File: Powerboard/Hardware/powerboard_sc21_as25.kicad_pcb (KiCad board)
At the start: 4 copper layers, 86.3 x 55.6 mm, 152 parts, among them IC1 BQ24618RGET-iclr, IC2 CP2102, J1 Thermistor Connection 103AT N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, J10 Conn_01x04_Male, J11 Conn_01x03_MountingPin, J2 Conn_01x02_Male, J3 Conn_01x02_Male, J4 Conn_01x08_Male, J5 Conn_01x04_Male, J6 Conn_01x02_Male, J7 IsolationSwitch, J8 USB_C_Receptacle_USB2.0, J9 Conn_Coaxial, Q1 RSJ250P10TL, Q10 MCH6351, Q2 RSJ250P10TL, Q3 RSJ250P10TL, Q4 RS1G120MN, Q5 RS1G120MN, Q6 MMDT2222A, Q7 RSJ250P10TL, Q8 RSJ250P10TL, Q9 MCH6351, U1 LTC4412xS6, U11 LTC4411, U2 SN65HVD230, U3 ESP32-PICO-D4, U4 SC4216H, U6 LM2679T-3.3-iclr, U7 LM2679T-3.3-iclr, U8 LTC4412xS6, U9 LTC4412xS6

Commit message: update
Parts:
- moved J7 7.10 mm to (78.6, 78.3), turned to 90 degrees
- moved J6 0.10 mm to (87.8, 71.1)
- moved C44 0.05 mm to (117.8, 69.0)
- moved C48 0.05 mm to (117.8, 70.5)
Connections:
- J7 pad 1: /Battery Charger/Q3-D -> Net-(C31-Pad1)
- J7 pad 2: Net-(C31-Pad1) -> /Battery Charger/Q3-D
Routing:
- net Net-(C31-Pad1): track 38.8 -> 29.7 mm
- net /Battery Charger/Q3-D: track 76.0 -> 74.4 mm, vias 4 -> 3

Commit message: update
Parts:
- added TP1: TestPoint, TestPoint:TestPoint_Pad_D1.5mm, B.Cu at (86.8, 58.0)
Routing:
- net Net-(C31-Pad1): track 29.7 -> 38.9 mm
- net GND: track 103.7 -> 107.9 mm
- net /LPC_24V: track 9.98 -> 12.6 mm
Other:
- board text added: "ISOLATOR"
- board text removed: "ISOLATION SWITCH"

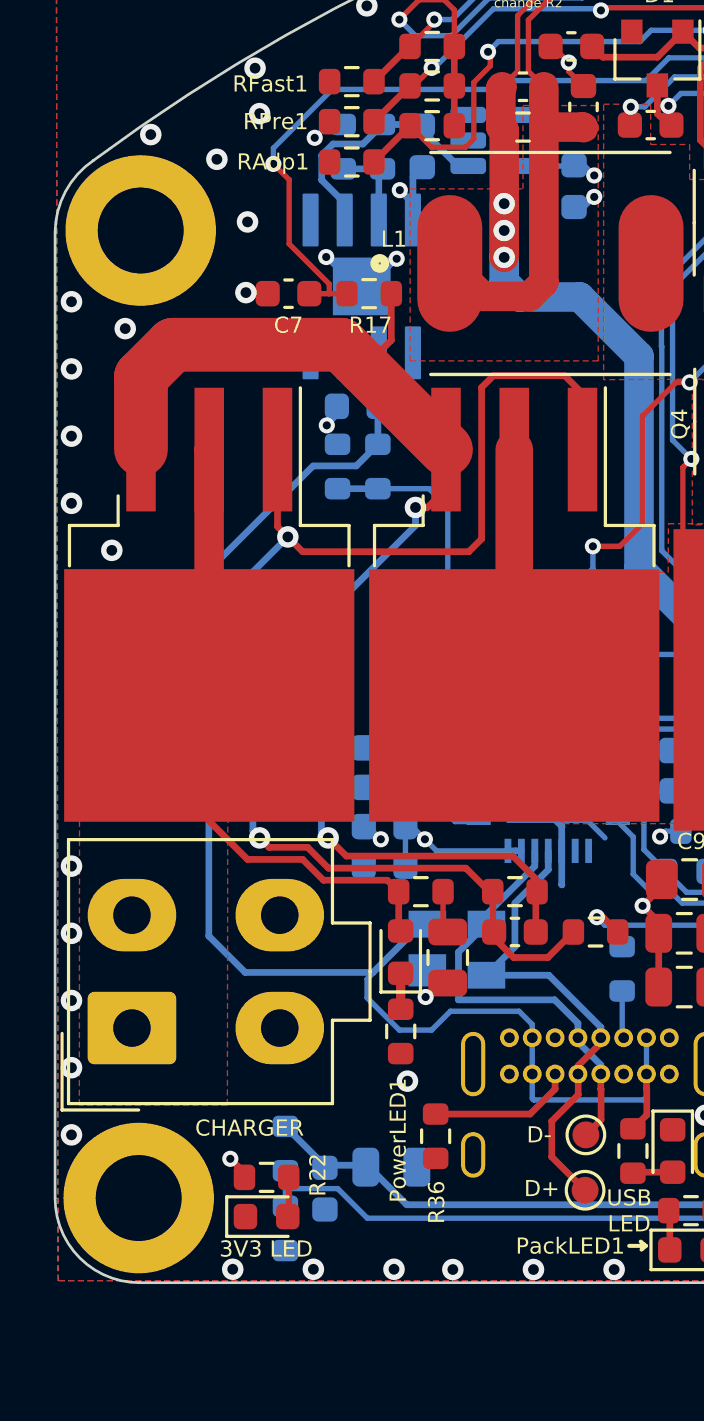
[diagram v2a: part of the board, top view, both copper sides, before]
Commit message: Changed input filter resistors and changed layout to match
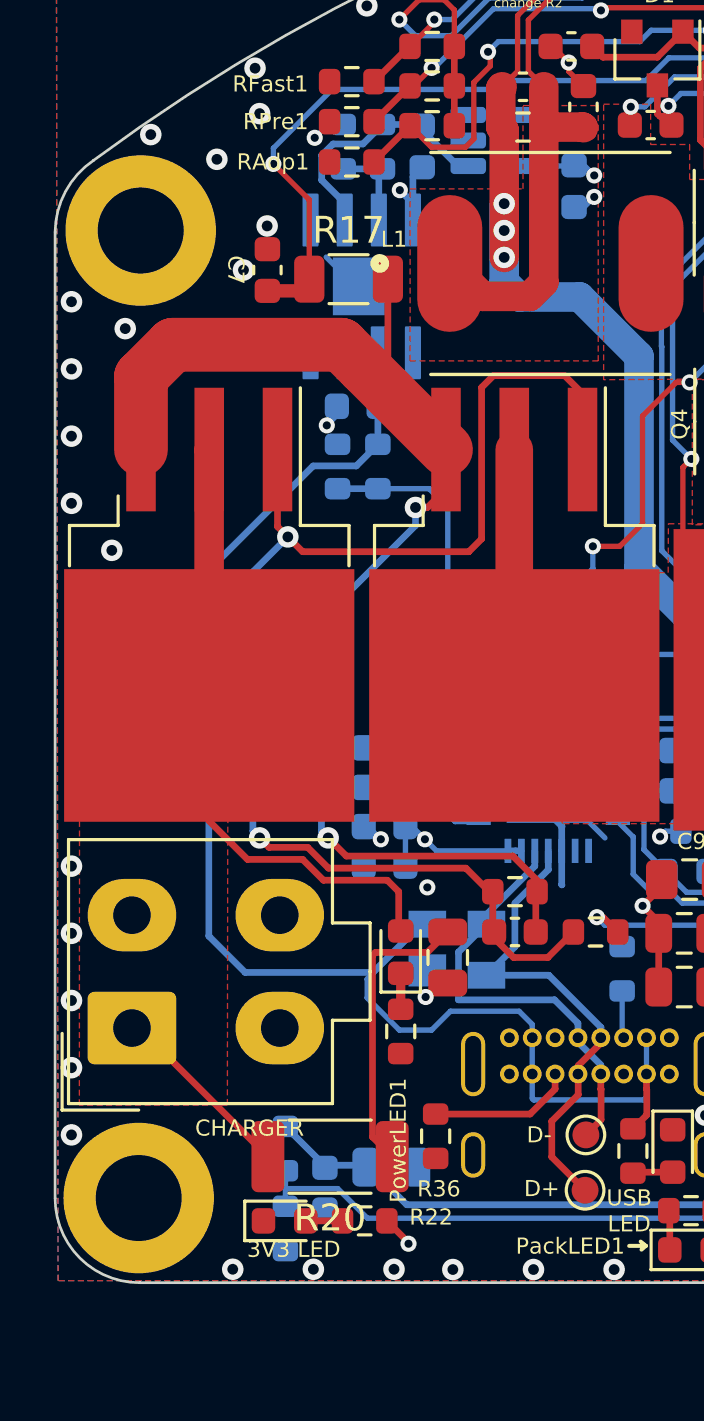
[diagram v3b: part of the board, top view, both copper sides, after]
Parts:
- R17: footprint Resistor_SMD:R_0603_1608Metric -> Resistor_SMD:R_1206_3216Metric
- R20: footprint Resistor_SMD:R_0603_1608Metric -> Resistor_SMD:R_2010_5025Metric
- moved R20 10.4 mm to (59.1, 78.3)
- moved R22 3.99 mm to (60.4, 80.7), turned to 0 degrees
- moved C7 1.18 mm to (56.8, 45.3), turned to -90 degrees
- moved R17 0.94 mm to (59.8, 45.7)
- moved D9 0.69 mm to (57.4, 80.7)
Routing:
- net Net-(C16-Pad1): track 1.33 -> 11.0 mm
- net Net-(J5-Pad1): track 20.9 -> 28.0 mm
- net /Battery Charger/Q1-S: track 44.9 -> 46.0 mm
- net /Battery Charger/VCC: track 30.4 -> 29.9 mm
- net GND: vias 157 -> 155

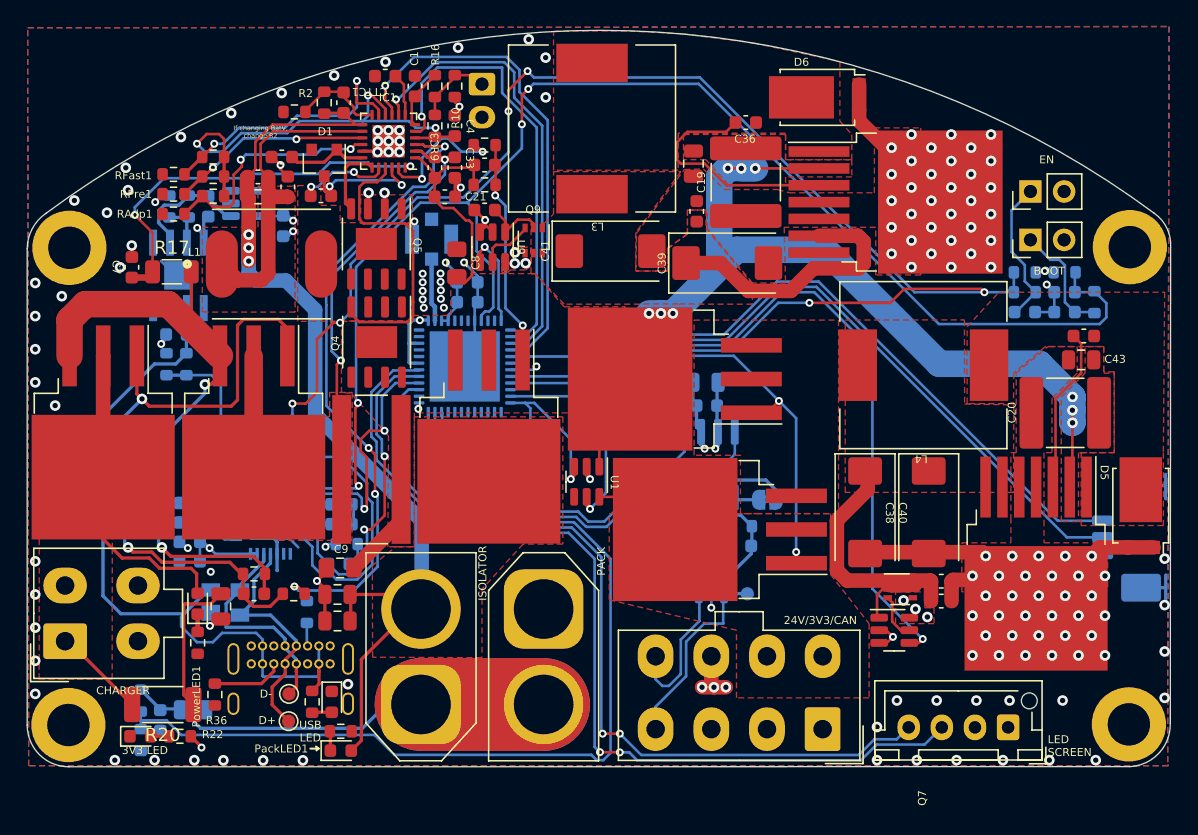
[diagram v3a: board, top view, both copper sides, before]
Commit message: updated pins and new layout
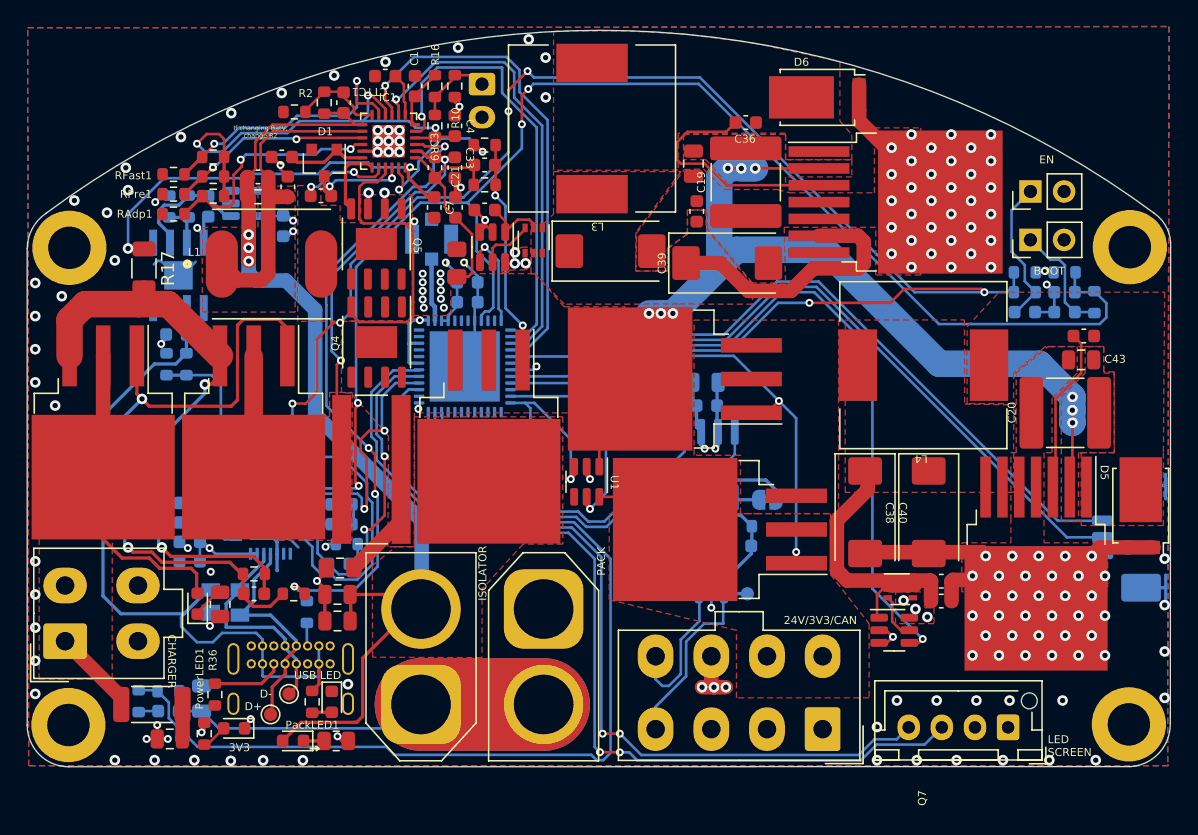
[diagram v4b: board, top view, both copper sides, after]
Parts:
- R28, R29: footprint Resistor_SMD:R_0603_1608Metric -> Resistor_SMD:R_0805_2012Metric
- moved C7 23.3 mm to (79.6, 40.8), turned to 90 degrees
- moved C16 10.7 mm to (59.6, 80.9), turned to 180 degrees
- moved D9 7.10 mm to (64.5, 80.1), turned to 180 degrees
- moved PackLED1 3.67 mm to (69.0, 81.0), turned to 180 degrees
- moved R29 3.36 mm to (63.5, 70.8)
- moved R31 2.93 mm to (57.3, 78.0)
- moved R30 2.21 mm to (59.5, 77.3), turned to 180 degrees
- moved R17 2.13 mm to (57.7, 45.4), turned to -90 degrees
- moved R22 1.85 mm to (62.2, 80.5), turned to 90 degrees
- moved TP24 1.45 mm to (67.2, 79.0)
- moved C21 1.13 mm to (81.2, 40.8), turned to 90 degrees
- moved C32 1.07 mm to (62.0, 77.8), turned to 90 degrees
- moved C31 0.94 mm to (59.5, 78.8), turned to 180 degrees
- moved R20 0.82 mm to (58.3, 78.3)
- moved R28 0.81 mm to (72.2, 81.0)
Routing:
- net Net-(C16-Pad1): track 11.0 -> 2.61 mm
- net GND: track 107.9 -> 113.9 mm, vias 155 -> 159
- net /Battery Charger/Q3-D: track 74.4 -> 78.2 mm
- net /Battery Charger/Q1-S: track 46.0 -> 43.1 mm
- net /Battery Charger/BTST: track 9.90 -> 8.27 mm
- net Net-(IC1-Pad23): track 10.2 -> 11.3 mm
- net /USB To UART/D+: track 17.8 -> 16.8 mm
- net Net-(PowerLED1-Pad1): track 1.34 -> 2.21 mm
- net /Battery Charger/VCC: track 29.9 -> 30.6 mm
- net Net-(C31-Pad1): track 38.9 -> 39.6 mm
- net Net-(D9-Pad2): track 1.37 -> 1.97 mm
- net Net-(J5-Pad1): track 28.0 -> 27.5 mm
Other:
- board text added: "3V3"
- board text removed: "3V3 LED"
